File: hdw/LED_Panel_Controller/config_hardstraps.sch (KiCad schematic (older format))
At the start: 19 parts, among them J1201 PIC_UART, J1202 WIFI_UART, J1203 I2C, J1204 WIFI_SPI, J1205 SD_SPI, J1206 FLASH_SPI, U1201 MCP9804

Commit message: having a mid-project crisis
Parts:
- removed J1202: WIFI_UART, Connector_PinHeader_2.54mm:PinHeader_1x03_P2.54mm_Vertical, symbol Connector_Generic:Conn_01x03
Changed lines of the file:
@@
 	0    1    -1   0
 $EndComp
-Wire Wire Line
-	4740 5870 4820 5870
-Wire Wire Line
-	4740 5950 4740 5870
-$Comp
-L power:GND #PWR01215
-U 1 1 6022B183
-P 4740 5950
-F 0 "#PWR01215" H 4740 5700 50  0001 C CNN
-F 1 "GND" H 4740 5800 50  0000 C CNN
-F 2 "" H 4740 5950 50  0001 C CNN
-F 3 "" H 4740 5950 50  0001 C CNN
-	1    4740 5950
-	1    0    0    -1
-$EndComp
-$Comp
-L Connector_Generic:Conn_01x03 J1202
-U 1 1 6022AEF7
-P 5020 5770
-F 0 "J1202" H 5020 5970 50  0000 C CNN
-F 1 "WIFI_UART" H 5020 5570 50  0000 C CNN
-F 2 "Connector_PinHeader_2.54mm:PinHeader_1x03_P2.54mm_Vertical" H 5020 5770 50  0001 C CNN
-F 3 "~" H 5020 5770 50  0001 C CNN
-F 4 "DNP" H 5020 5770 50  0001 C CNN "Configuration"
-	1    5020 5770
-	1    0    0    -1
-$EndComp
-Text GLabel 4820 5770 0    50   UnSpc ~ 0
-WIFI_UART_TX
-Text GLabel 4820 5670 0    50   UnSpc ~ 0
-WIFI_UART_RX
 Text GLabel 4820 5020 0    50   UnSpc ~ 0
 PIC32MZ_UART_TX

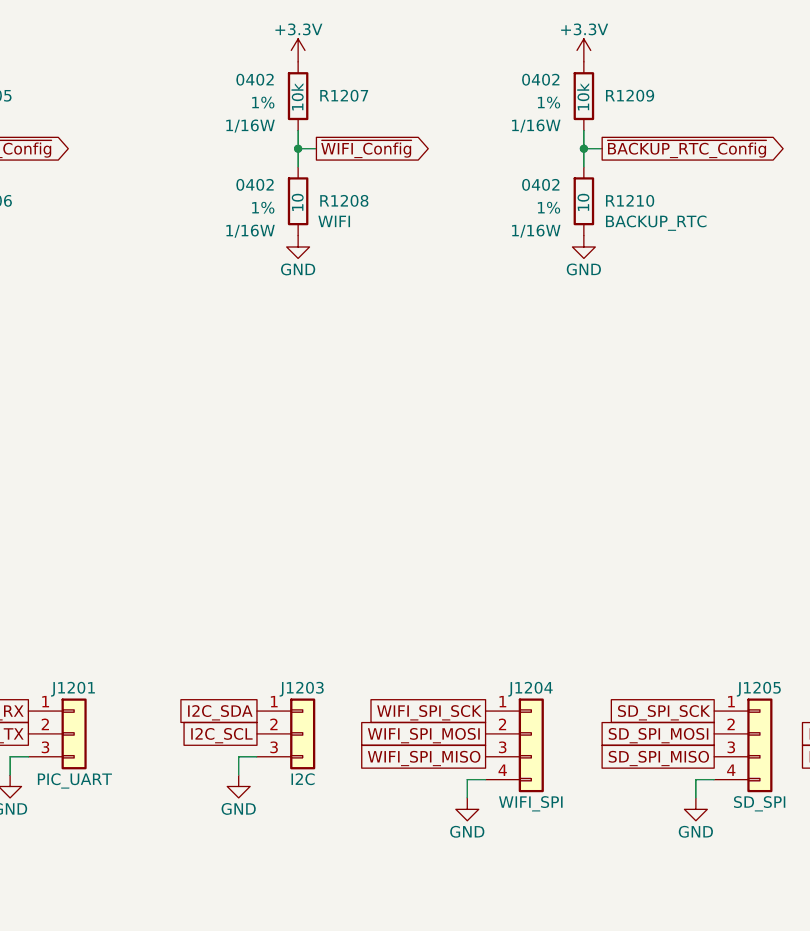
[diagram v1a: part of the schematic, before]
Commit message: reworked schematic to use MLVDS connector instead of wifi module
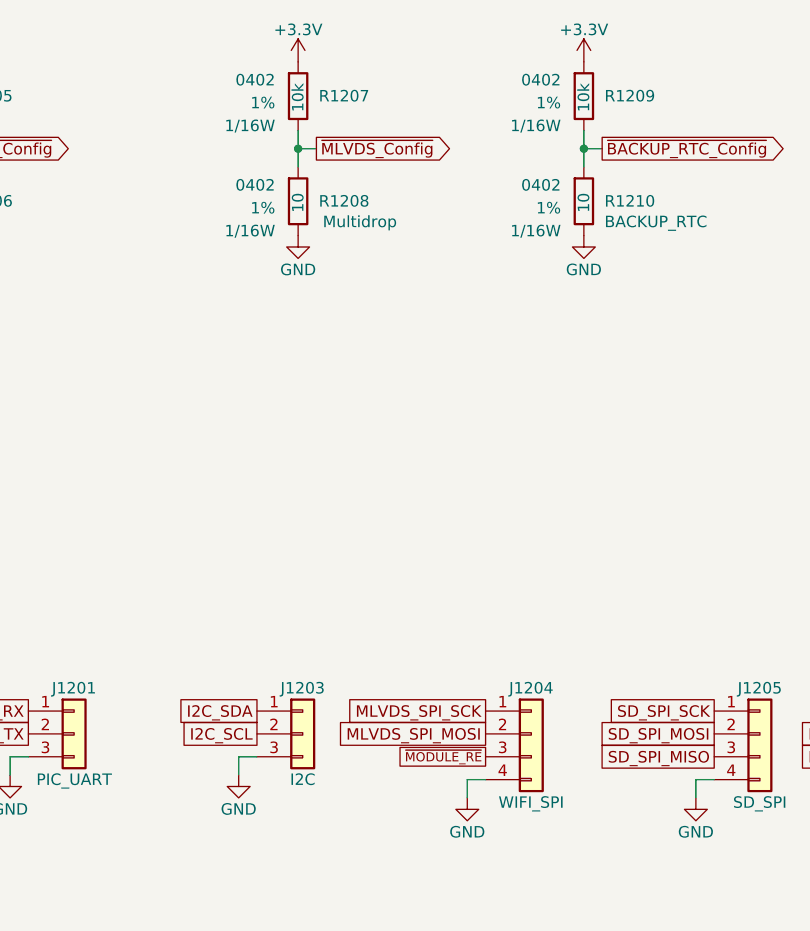
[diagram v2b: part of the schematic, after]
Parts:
- R1208: Configuration WIFI -> Multidrop
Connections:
- net WIFI_SPI_MISO renamed ~MODULE_RE
- net WIFI_SPI_MOSI renamed MLVDS_SPI_MOSI
- net WIFI_SPI_SCK renamed MLVDS_SPI_SCK
- net ~WIFI_Config renamed ~MLVDS_Config
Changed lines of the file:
@@
 Sheet 12 34
 Title "LED Panel Controller"
-Date "2021-03-31"
+Date "2021-05-30"
 Rev "A"
 Comp "Drew Maatman"
@@
 F 5 "1%" H 6100 2660 50  0000 L CNN "Tolerance"
 F 6 "1/16W" H 6100 2560 50  0000 L CNN "Wattage"
-F 7 "WIFI" H 5840 2600 50  0000 C CNN "Configuration"
+F 7 "Multidrop" H 5730 2600 50  0000 C CNN "Configuration"
 F 8 "RMCF0402FT10R0CT-ND" H 6000 2690 50  0001 C CNN "Digi-Key PN"
 	1    6000 2690
@@
 	6000 2540 6000 2460
 Text GLabel 6080 2460 2    50   Output ~ 0
-~WIFI_Config
+~MLVDS_Config
 Wire Wire Line
 	6080 2460 6000 2460
@@
 Text GLabel 7820 5020 0    50   UnSpc ~ 0
 SD_SPI_MOSI
-Text GLabel 6820 5120 0    50   UnSpc ~ 0
-WIFI_SPI_MISO
-Text GLabel 6820 5020 0    50   UnSpc ~ 0
-WIFI_SPI_MOSI
-Text GLabel 6820 4920 0    50   UnSpc ~ 0
-WIFI_SPI_SCK
 Wire Wire Line
 	6740 5220 6820 5220
@@
 	1    0    0    -1
 $EndComp
+Text GLabel 6820 4920 0    50   UnSpc ~ 0
+MLVDS_SPI_SCK
+Text GLabel 6820 5020 0    50   UnSpc ~ 0
+MLVDS_SPI_MOSI
+Text GLabel 6820 5120 0    40   UnSpc ~ 0
+~MODULE_RE
 $EndSCHEMATC

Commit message: added BOMs, some consolidation
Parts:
- C1201: Digi-Key PN 490-10701-1-ND -> 490-10698-1-ND
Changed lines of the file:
@@
 F 6 "X7R" H 2370 6950 50  0000 R CNN "Dielectric"
 F 7 "Telemetry" H 2370 7240 50  0000 R CNN "Configuration"
-F 8 "490-10701-1-ND" H 2520 7090 50  0001 C CNN "Digi-Key PN"
+F 8 "490-10698-1-ND" H 2520 7090 50  0001 C CNN "Digi-Key PN"
 	1    2520 7090
 	1    0    0    -1
